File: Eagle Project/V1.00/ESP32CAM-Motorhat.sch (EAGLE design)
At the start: 21 parts, among them J1 10103594, J2 2p-smd-1.0-90d, J3 2p-smd-1.0-90d, J4 2p-2.0, SW1 SKQGADE010, U1 ESP32-DEVKITC-32D, U2 MX1508, U3 MP2307DN-LF, U4 CH340G

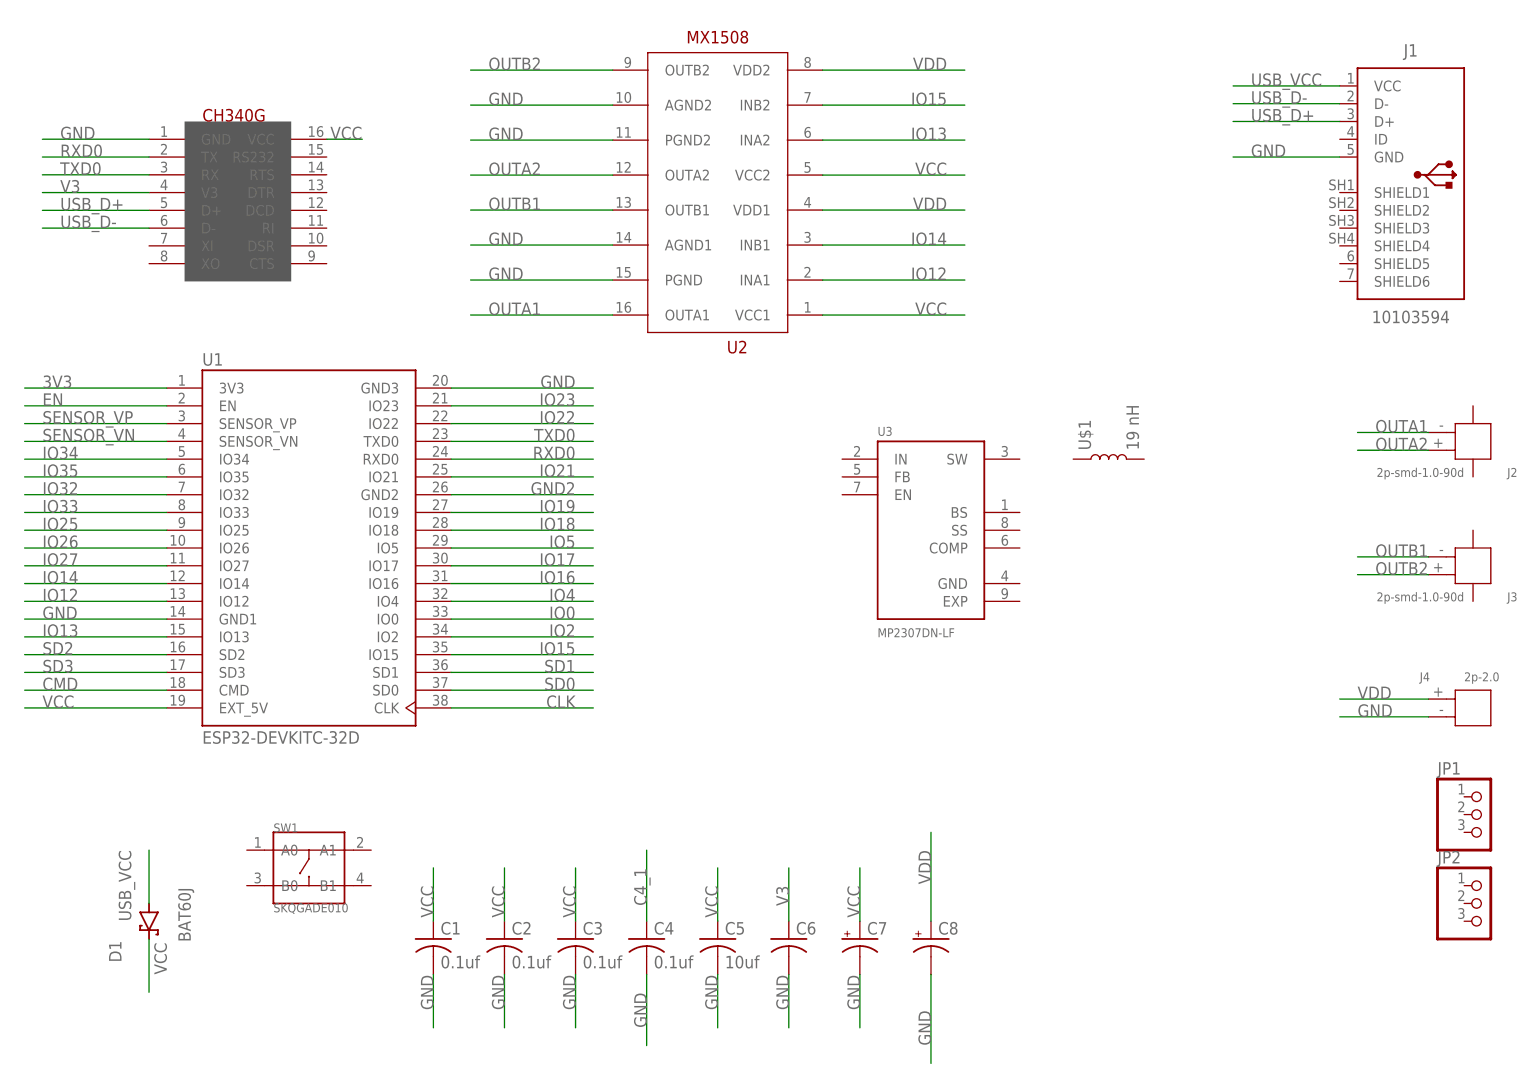
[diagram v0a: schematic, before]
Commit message: Power Supply is mostly complete. USB to Serial is mostly complete. H-Bridge still needs flywheel diodes. Footprint for ESP32 is completely wrong, editing the library footprint and pin allocation to match the ESP-CAM.
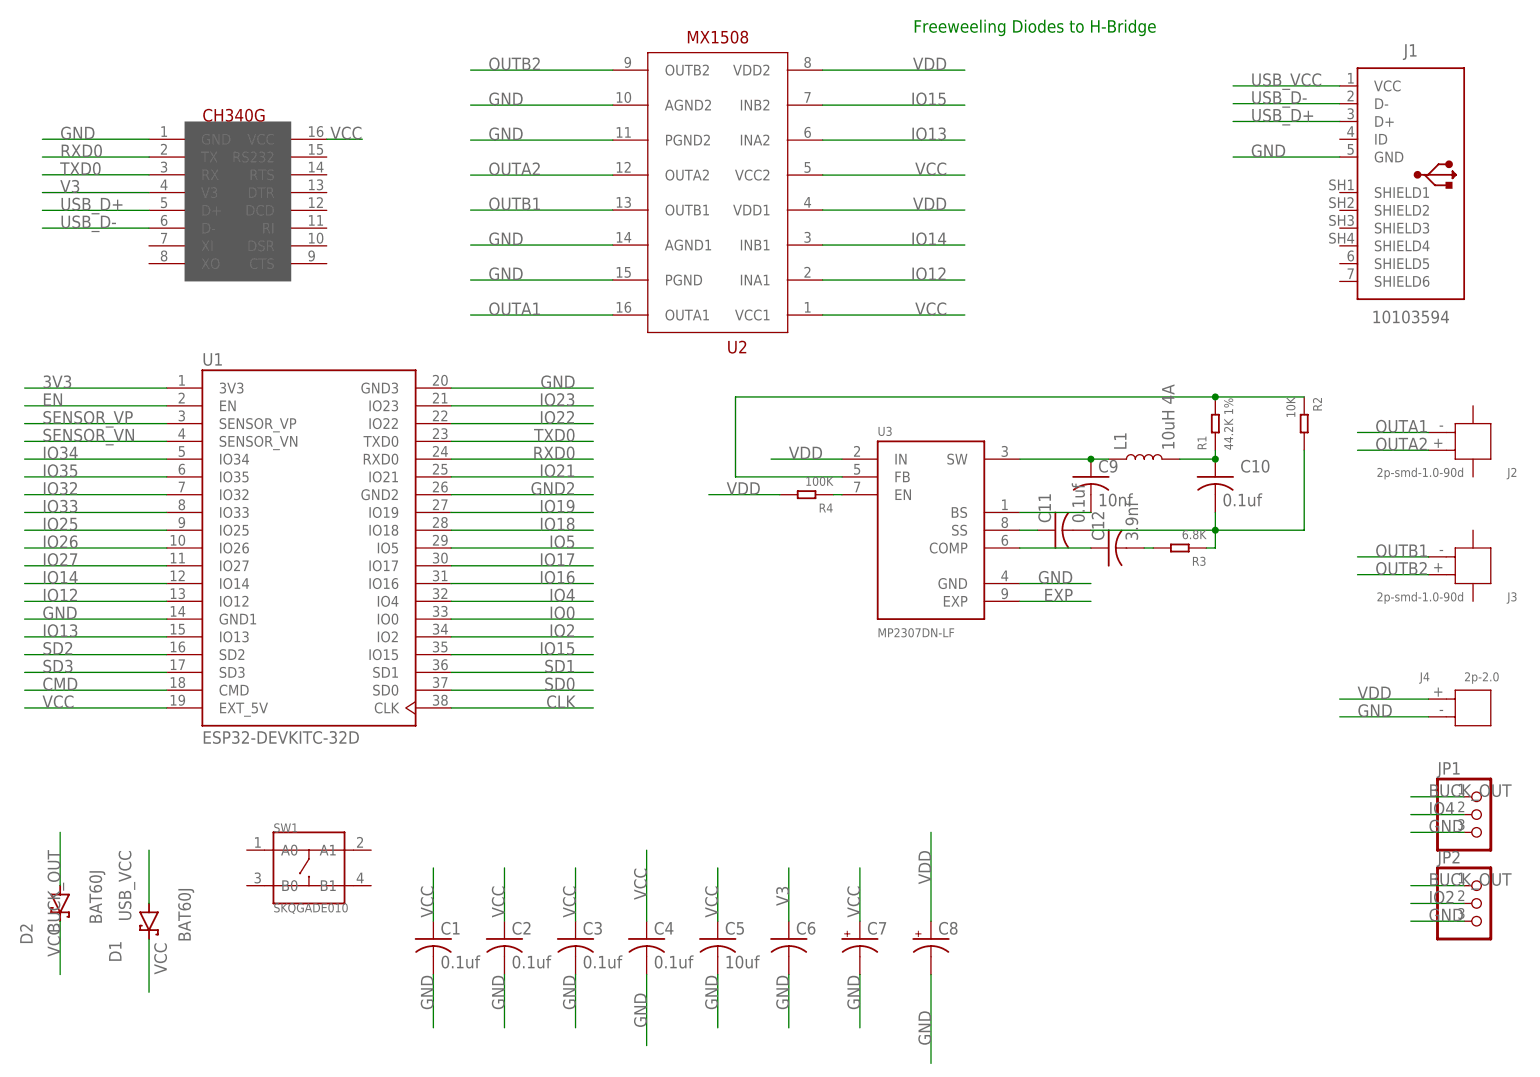
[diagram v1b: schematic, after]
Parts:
- removed U$1: 19 nH, SparkFun-Coils:19NH-0402
- added C10, C11: 0.1uf, adafruit:C-USC1206
- added C12: 3.9nf, adafruit:C-USC1206
- added C9: 10nf, adafruit:C-USC1206
- added D2: BAT60J, diode:BAT60J
- added L1: 10uH 4A, SparkFun-Coils:19NH-0402
- added R1: 44.2K 1%, OPL_Resistor:SMD-RES-0R-1%-1/8W(0805)
- added R2: 10K, OPL_Resistor:SMD-RES-0R-1%-1/8W(0805)
- added R3: 6.8K, OPL_Resistor:SMD-RES-0R-1%-1/8W(0805)
- added R4: 100K, OPL_Resistor:SMD-RES-0R-1%-1/8W(0805)
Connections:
- removed net C4_1: C4.1
- new net BUCK_OUT: C10.1, D2.A, JP1.1, JP2.1, L1.2, R1.1
- new net EXP: U3.EXP
- new net N$1: C9.1, L1.1, U3.SW
- new net N$3: C9.2, U3.BS
- new net N$4: C11.1, U3.SS
- new net N$5: C10.2, C11.2, R2.2, R3.1
- new net N$6: R1.2, R2.1, U3.FB
- new net N$7: R4.1, U3.EN
- new net N$8: C12.1, U3.COMP
- new net N$9: C12.2, R3.2
- net GND: now also JP1.3, JP2.3, U3.GND
- net IO2: now also JP2.2
- net IO4: now also JP1.2
- net VCC: now also C4.1, D2.C
- net VDD: now also R4.2, U3.IN
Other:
- note added: "Freeweeling Diodes to H-Bridge"
